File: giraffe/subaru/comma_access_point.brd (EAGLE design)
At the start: 28.5 x 25.3 mm, 12 parts, among them J1 5018762640, J2 5018761040, J3 3-794618-2

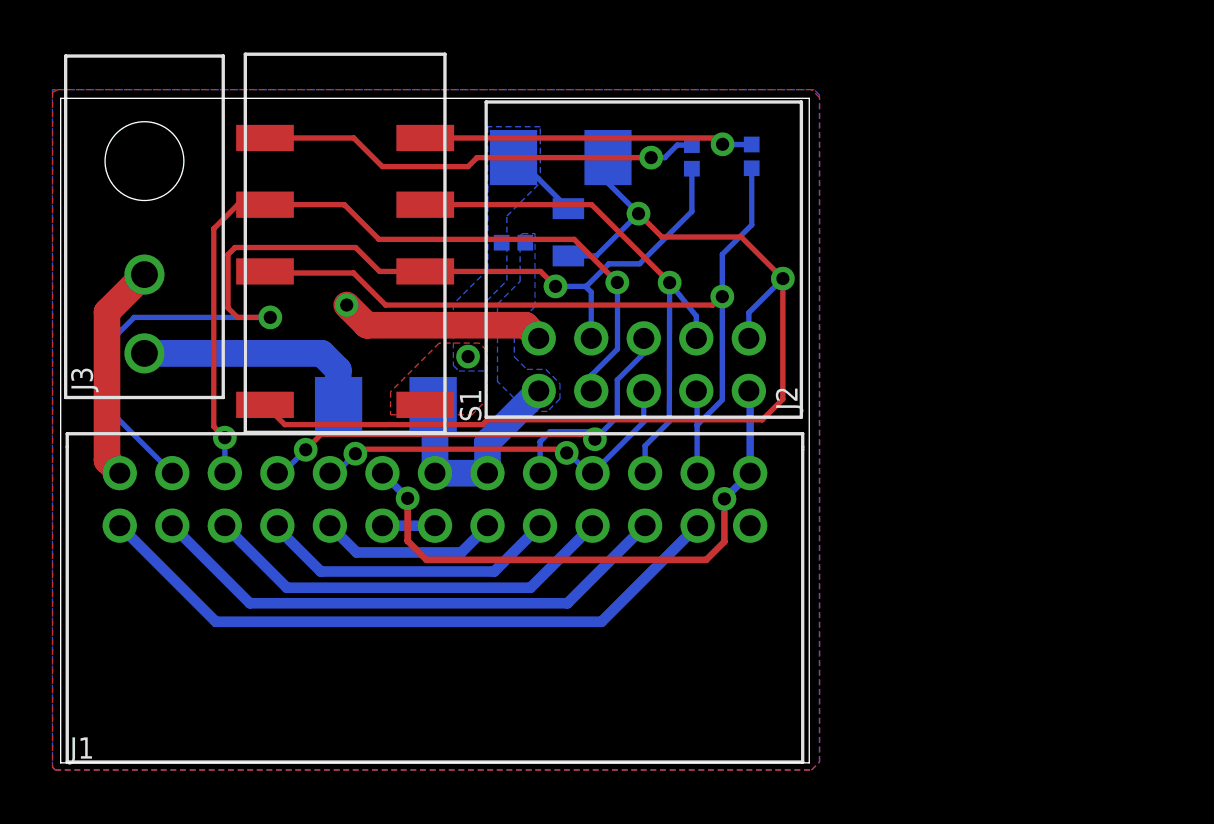
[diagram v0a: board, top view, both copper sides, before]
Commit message: added UJA1023 to subaru giraffe on mlp's request
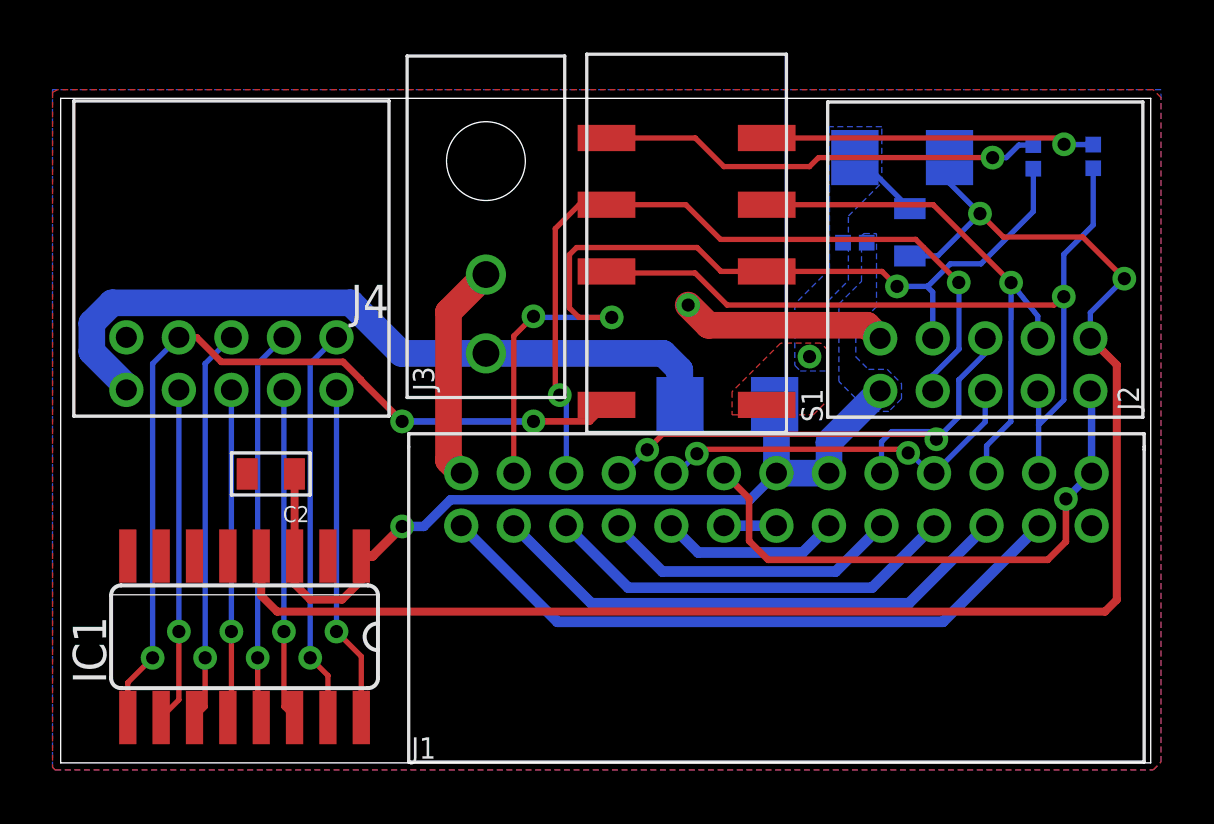
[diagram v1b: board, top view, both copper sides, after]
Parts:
- added C2: .1uF, comma.ai:0805-C
- added IC1: UJA1023, uja1023:SO16
- added J4: 5018761040, 5018761440:5018761040
- moved D1 13.0 mm to (32.0, 23.0)
- moved J2 13.0 mm to (36.2, 15.2)
- moved R1 13.0 mm to (39.3, 23.1)
- moved J3 13.0 mm to (16.2, 22.9)
- moved C1 13.0 mm to (32.3, 20.2)
- moved J1 13.0 mm to (27.2, 10.0)
- moved R2 13.0 mm to (37.0, 23.1)
- moved R4 13.0 mm to (30.2, 19.8)
- moved U$1 13.0 mm to (41.5, 1.57)
- moved D2 13.0 mm to (25.4, 13.6)
- moved S1 13.0 mm to (23.8, 20.0)
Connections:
- new net GPIO0: IC1.9, J4.P3, S1.P12
- new net GPIO1: IC1.10, J4.P4
- new net GPIO2: IC1.11, J4.P5
- new net GPIO3: IC1.12, J4.P6
- new net GPIO4: IC1.13, J4.P7
- new net GPIO5: IC1.14, J4.P8
- new net GPIO6: IC1.15, J4.P9
- new net GPIO7: IC1.16, J4.P10
- net 12VIN: now also C2.1, IC1.1, IC1.3
- net CAR_VIN: now also J4.P2
- net GND: now also C2.2, IC1.5, J4.P1
- net L_LINE: now also IC1.4; no longer S1.P12
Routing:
- net GPIO0: track 0.00 -> 33.2 mm, vias 0 -> 3
- net 12VIN: track 8.58 -> 33.9 mm, vias 0 -> 1
- net L_LINE: track 40.3 -> 60.2 mm
- net CAR_VIN: track 8.97 -> 28.2 mm
- net GPIO6: track 0.00 -> 15.2 mm, vias 0 -> 1
- net GPIO2: track 0.00 -> 15.1 mm, vias 0 -> 1
- net GPIO4: track 0.00 -> 14.9 mm, vias 0 -> 1
- net GPIO7: track 0.00 -> 12.9 mm, vias 0 -> 1
- net GPIO1: track 0.00 -> 12.8 mm, vias 0 -> 1
- net GPIO5: track 0.00 -> 12.6 mm, vias 0 -> 1
- net GPIO3: track 0.00 -> 12.5 mm, vias 0 -> 1
- net CAN_CAM_L: track 39.5 -> 36.3 mm, vias 2 -> 3
- net IGN: vias 2 -> 1
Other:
- board size 28.5 x 25.3 mm -> 41.5 x 25.3 mm
- board text added: "2019-08-31"
- board text removed: "3/21/19"
